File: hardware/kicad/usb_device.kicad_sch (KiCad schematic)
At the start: 3 parts, among them J2 USB-C_16P-F-SMT

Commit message: Refactor the microcontroller sheet; add switch footprint and 3d file; add titles, date and WaveRig annotation to all sheets.
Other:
- company: (none) -> WaveRig
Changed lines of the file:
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@@
 	(generator_version "10.0")
 	(paper "A4")
+	(title_block
+		(rev "0.1")
+		(company "WaveRig")
+	)
 	(wire
 		(pts

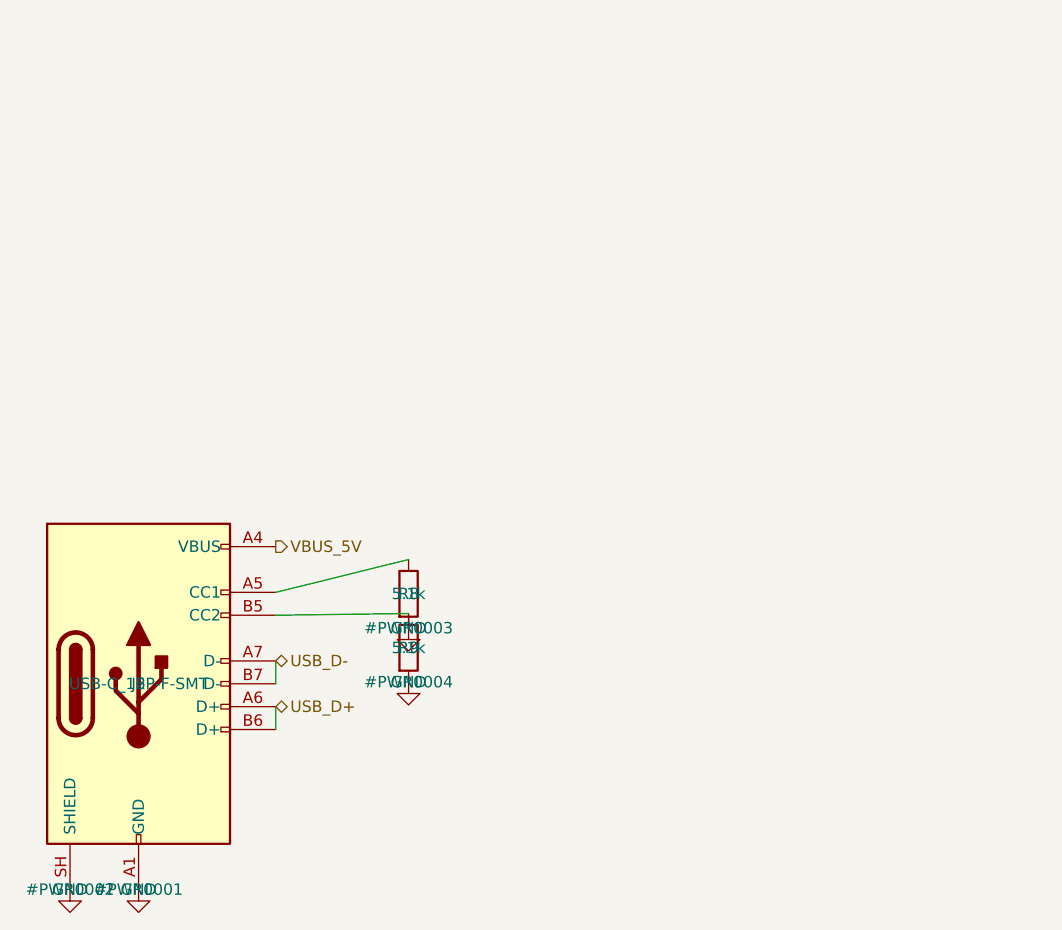
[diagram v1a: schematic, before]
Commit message: Refactor the USB connector sheet.
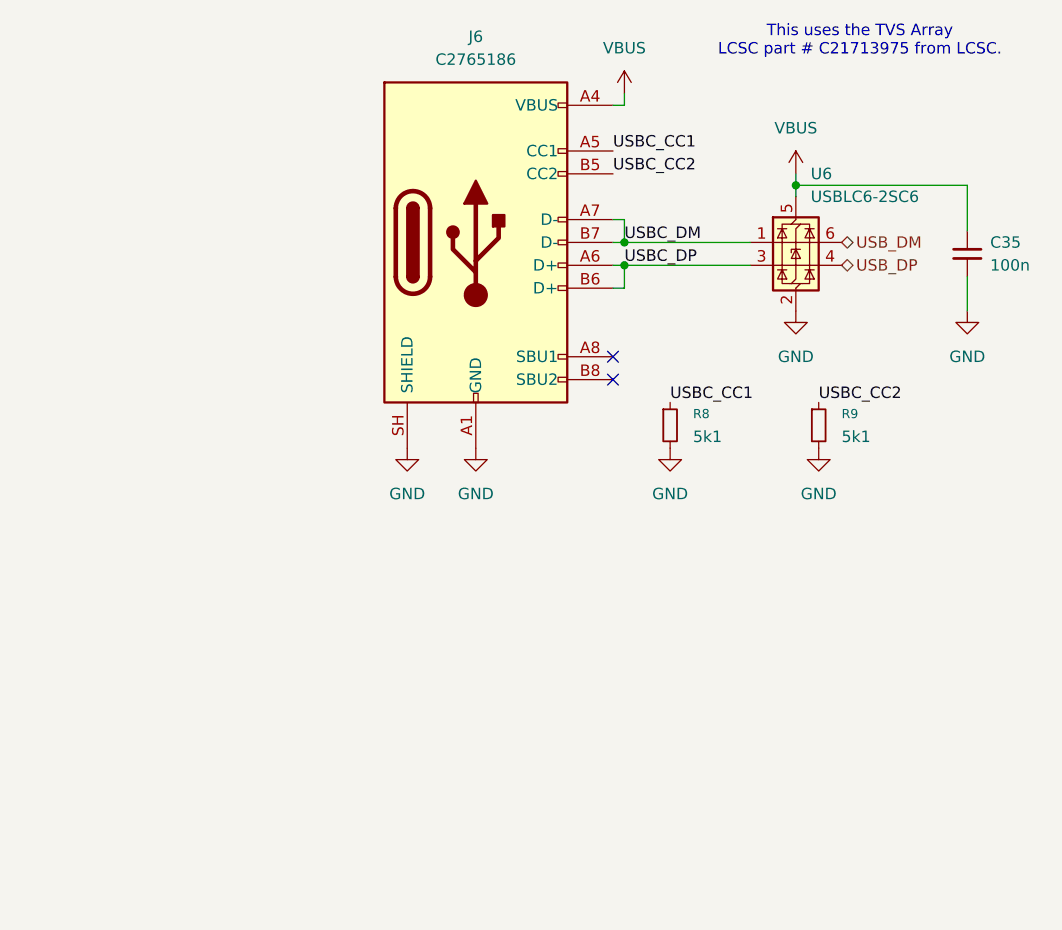
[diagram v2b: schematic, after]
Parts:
- removed J2: USB-C_16P-F-SMT, Connector_USB:USB_C_Receptacle_GCT_USB4115-03-C, symbol Connector:USB_C_Receptacle_USB2.0_14P
- removed R8, R9: 5.1k, Resistor_SMD:R_0603_1608Metric, symbol Device:R
- added C35: 100n, Capacitor_SMD:C_0603_1608Metric, symbol Device:C_Small
- added J6: C2765186, Connector_USB:USB_C_Receptacle_GCT_USB4115-03-C, symbol Connector:USB_C_Receptacle_USB2.0_16P
- added R8, R9: 5k1, Resistor_SMD:R_0603_1608Metric, symbol Device:R_Small
- added U6: USBLC6-2SC6, Package_TO_SOT_SMD:SOT-23-6, symbol Power_Protection:USBLC6-2SC6
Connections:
- net GND: now also C35.1, J6.A1 (GND), J6.A12 (GND), J6.B1 (GND), J6.B12 (GND), J6.SH (SHIELD), R8.2, R9.2, U6.2 (GND)
- new net USBC_CC1: J6.A5 (CC1), R8.1
- new net USBC_CC2: J6.B5 (CC2), R9.1
- new net USBC_DM: J6.A7 (D-), J6.B7 (D-), U6.1 (I/O1)
- new net USBC_DP: J6.A6 (D+), J6.B6 (D+), U6.3 (I/O2)
- new net USB_DM: U6.6 (I/O1)
- new net USB_DP: U6.4 (I/O2)
- new net VBUS: C35.2, J6.A4 (VBUS), J6.A9 (VBUS), J6.B4 (VBUS), J6.B9 (VBUS), U6.5 (VBUS)
- no-connect marks 0 -> 2
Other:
- note added: "This uses the TVS Array LCSC part # C21713975 from LCSC."
- title: (none) -> USB Type-C Connector Assy
